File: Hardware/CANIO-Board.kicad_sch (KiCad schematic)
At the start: 0 parts

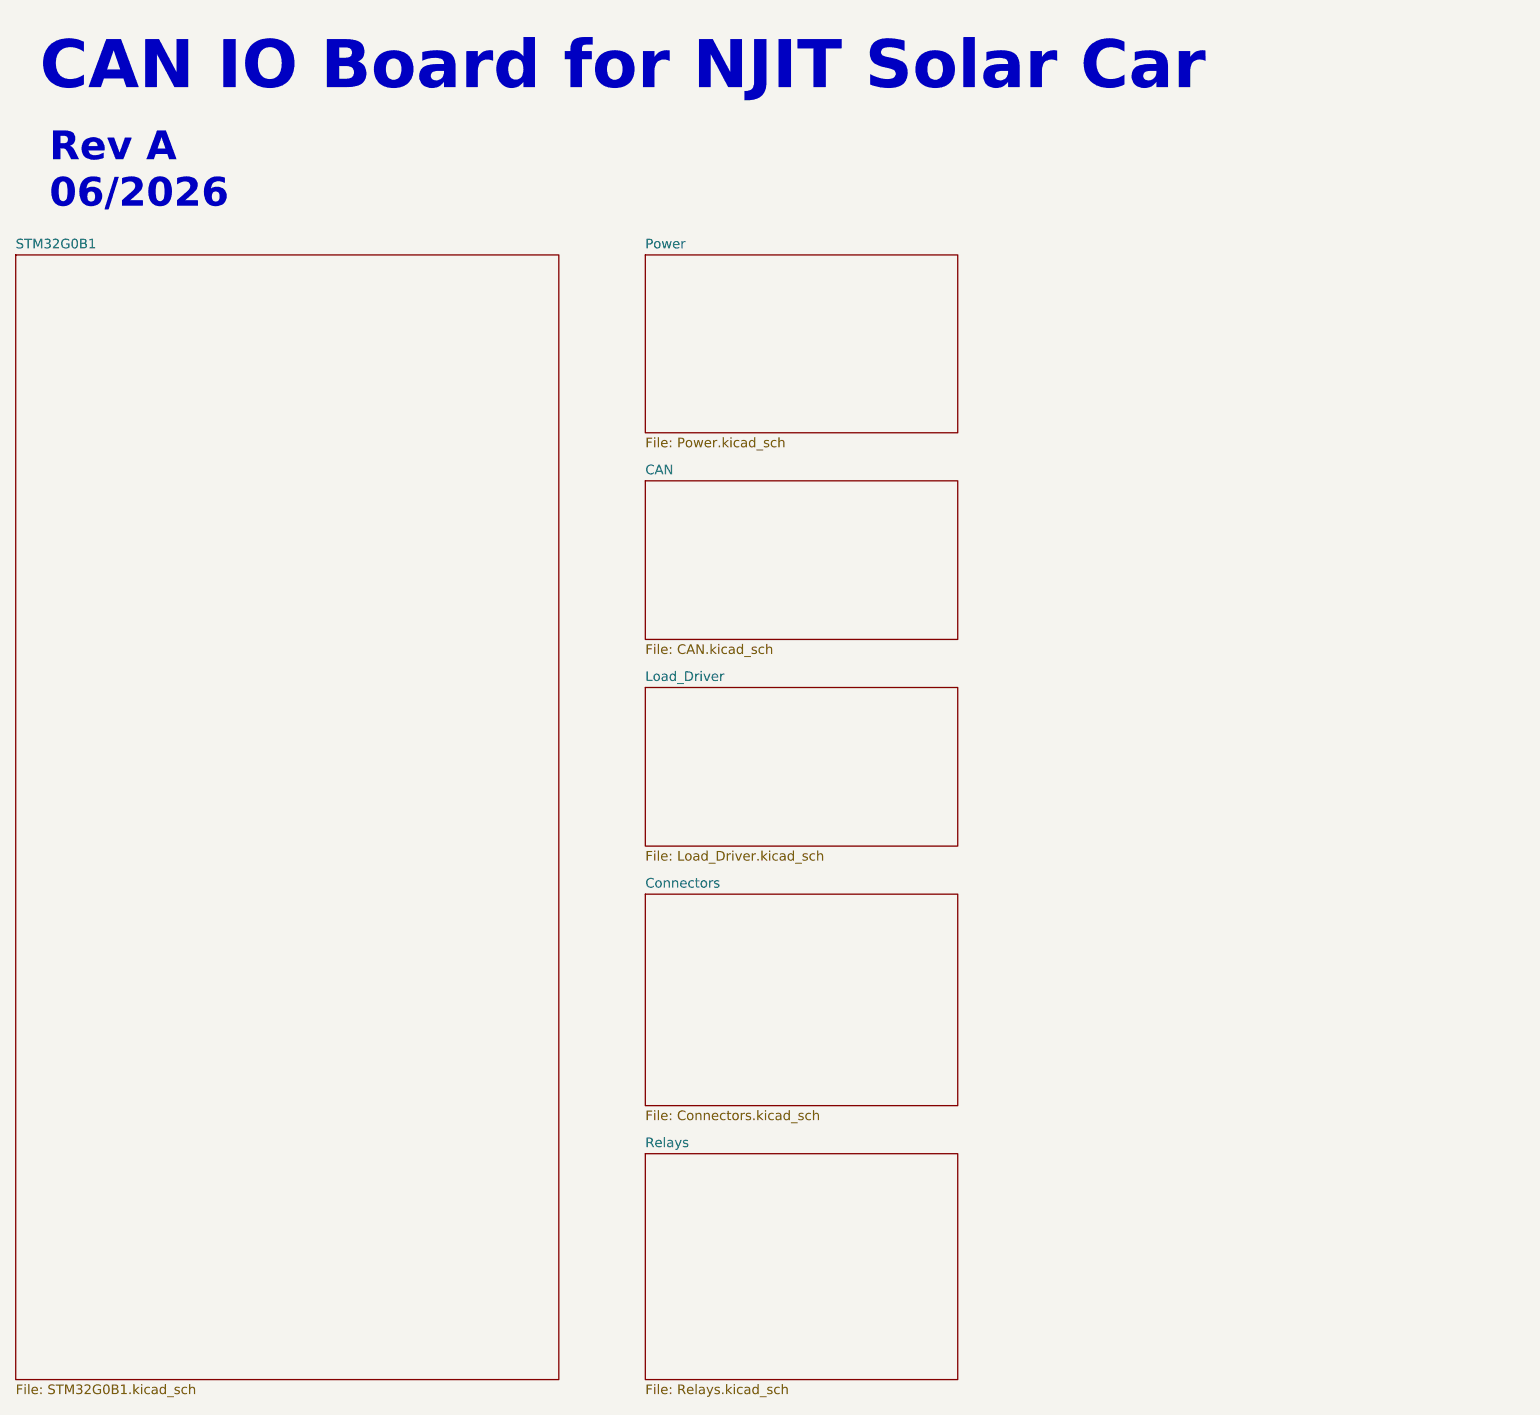
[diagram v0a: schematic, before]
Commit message: Added Relay Driver schematics
- added the ICs, relay sockets, etc
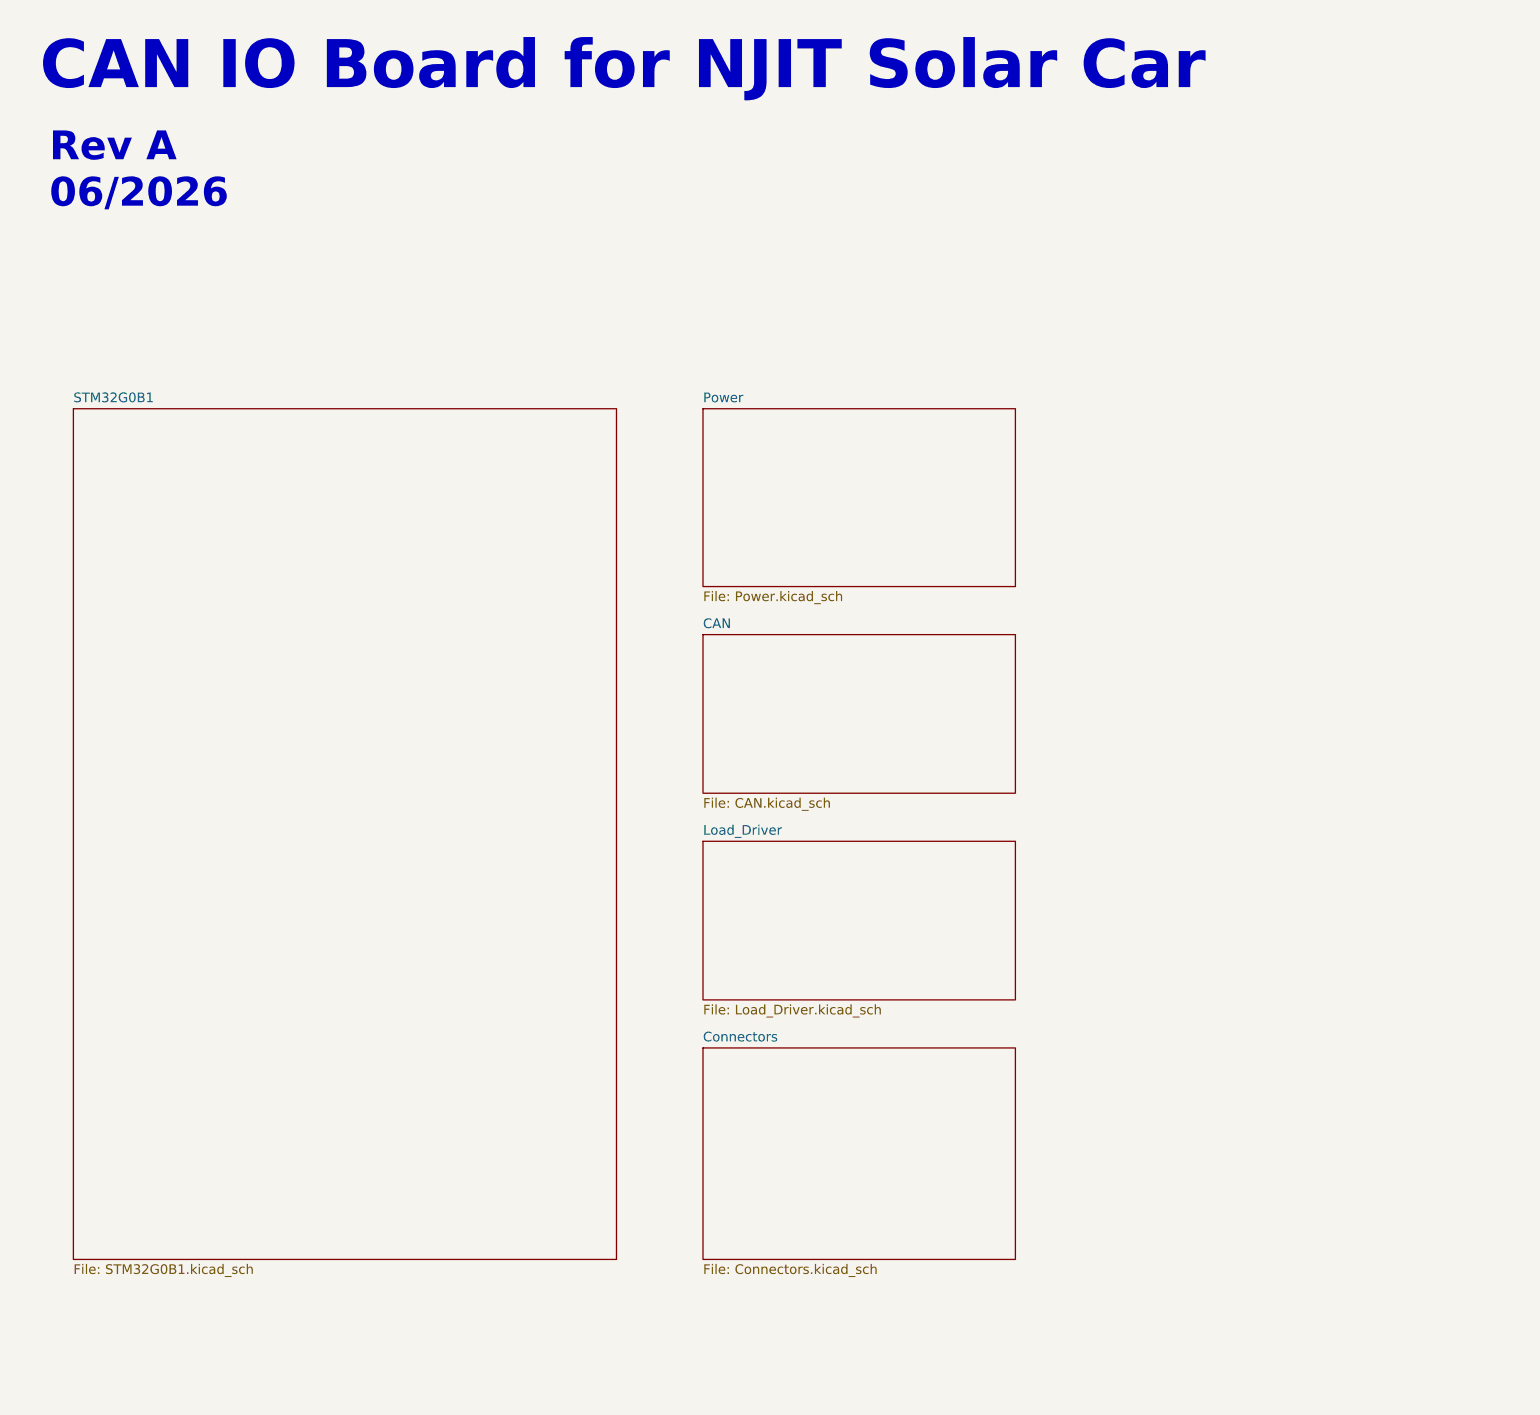
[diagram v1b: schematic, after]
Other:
- removed sheet Relays
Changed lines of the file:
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@@
 	)
 	(sheet
-		(at 100.33 108.585)
+		(at 107.95 128.905)
 		(size 41.275 20.955)
 		(exclude_from_sim no)
@@
 		)
 		(property "Sheetname" "Load_Driver"
-			(at 100.33 107.8734 0)
+			(at 107.95 128.1934 0)
 			(effects
 				(font
@@
 		)
 		(property "Sheetfile" "Load_Driver.kicad_sch"
-			(at 100.33 130.1246 0)
+			(at 107.95 150.4446 0)
 			(effects
 				(font
@@
 	)
 	(sheet
-		(at 17.145 51.435)
-		(size 71.755 148.59)
+		(at 24.765 71.755)
+		(size 71.755 112.395)
 		(exclude_from_sim no)
 		(in_bom yes)
@@
 		)
 		(property "Sheetname" "STM32G0B1"
-			(at 17.145 50.7234 0)
+			(at 24.765 71.0434 0)
 			(effects
 				(font
@@
 		)
 		(property "Sheetfile" "STM32G0B1.kicad_sch"
-			(at 17.145 200.6096 0)
+			(at 24.765 184.7346 0)
 			(effects
 				(font
@@
 	)
 	(sheet
-		(at 100.33 51.435)
+		(at 107.95 71.755)
 		(size 41.275 23.495)
 		(exclude_from_sim no)
@@
 		)
 		(property "Sheetname" "Power"
-			(at 100.33 50.7234 0)
+			(at 107.95 71.0434 0)
 			(effects
 				(font
@@
 		)
 		(property "Sheetfile" "Power.kicad_sch"
-			(at 100.33 75.5146 0)
+			(at 107.95 95.8346 0)
 			(effects
 				(font
@@
 	)
 	(sheet
-		(at 100.33 170.18)
-		(size 41.275 29.845)
-		(exclude_from_sim no)
-		(in_bom yes)
-		(on_board yes)
-		(dnp no)
-		(fields_autoplaced yes)
-		(stroke
-			(width 0.1524)
-			(type solid)
-		)
-		(fill
-			(color 202 202 255 1.0000)
-		)
-		(property "Sheetname" "Relays"
-			(at 100.33 169.4684 0)
-			(effects
-				(font
-					(size 1.27 1.27)
-				)
-				(justify left bottom)
-			)
-		)
-		(property "Sheetfile" "Relays.kicad_sch"
-			(at 100.33 200.6096 0)
-			(effects
-				(font
-					(size 1.27 1.27)
-				)
-				(justify left top)
-			)
-		)
-		(instances
-			(project "CANIO-Board"
-				(path "/a11f98b2-3b09-4cf9-8535-19e509fe91b9"
-					(page "7")
-				)
-			)
-		)
-	)
-	(sheet
-		(at 100.33 135.89)
+		(at 107.95 156.21)
 		(size 41.275 27.94)
 		(exclude_from_sim no)
@@
 		)
 		(property "Sheetname" "Connectors"
-			(at 100.33 135.1784 0)
+			(at 107.95 155.4984 0)
 			(effects
 				(font
@@
 		)
 		(property "Sheetfile" "Connectors.kicad_sch"
-			(at 100.33 164.4146 0)
+			(at 107.95 184.7346 0)
 			(effects
 				(font
@@
 	)
 	(sheet
-		(at 100.33 81.28)
+		(at 107.95 101.6)
 		(size 41.275 20.955)
 		(exclude_from_sim no)
@@
 		)
 		(property "Sheetname" "CAN"
-			(at 100.33 80.5684 0)
+			(at 107.95 100.8884 0)
 			(effects
 				(font
@@
 		)
 		(property "Sheetfile" "CAN.kicad_sch"
-			(at 100.33 102.8196 0)
+			(at 107.95 123.1396 0)
 			(effects
 				(font

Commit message: Finished the ISOW1044 Schematic
- Ported over Kostadin's schematic

Co-authored-by: Kostadin Madjovski <155325994+bivein@users.noreply.github.com>
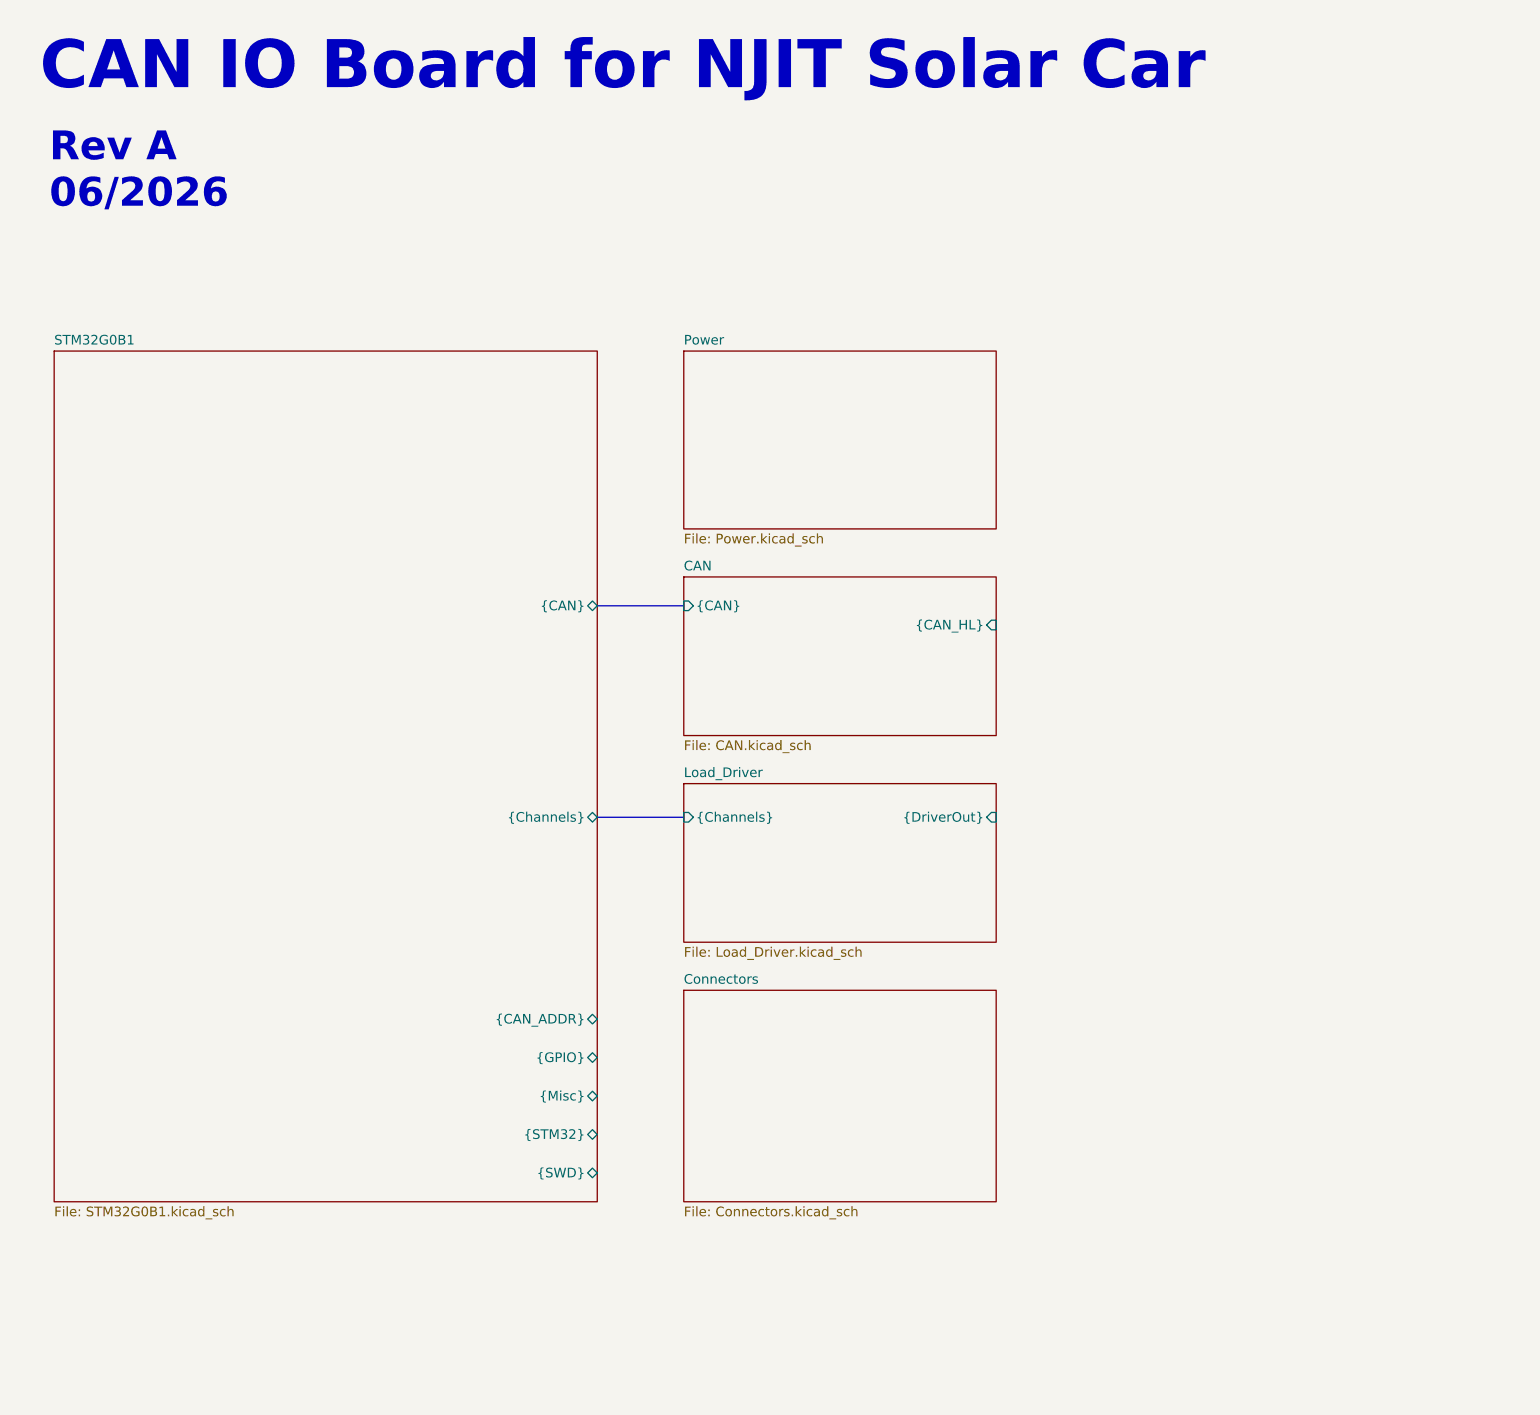
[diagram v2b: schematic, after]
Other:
- sheet CAN ports: added {CAN_HL}, {CAN}; removed none
- sheet Load_Driver ports: added {Channels}, {DriverOut}; removed none
- sheet STM32G0B1 ports: added {CAN_ADDR}, {CAN}, {Channels}, {GPIO}, {Misc}, {STM32}, {SWD}; removed none
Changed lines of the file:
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@@
+		)
+	)
+	(bus
+		(pts
+			(xy 93.98 97.79) (xy 105.41 97.79)
+		)
+		(stroke
+			(width 0)
+			(type default)
+		)
+	)
+	(bus
+		(pts
+			(xy 93.98 125.73) (xy 105.41 125.73)
+		)
+		(stroke
+			(width 0)
+			(type default)
 		)
 	)
@@
 	)
 	(sheet
-		(at 107.95 128.905)
+		(at 105.41 121.285)
 		(size 41.275 20.955)
 		(exclude_from_sim no)
@@
 		)
 		(property "Sheetname" "Load_Driver"
-			(at 107.95 128.1934 0)
+			(at 105.41 120.5734 0)
 			(effects
 				(font
@@
 		)
 		(property "Sheetfile" "Load_Driver.kicad_sch"
-			(at 107.95 150.4446 0)
+			(at 105.41 142.8246 0)
 			(effects
 				(font
@@
 				)
 				(justify left top)
+			)
+		)
+		(pin "{Channels}" input
+			(at 105.41 125.73 180)
+			(effects
+				(font
+					(size 1.27 1.27)
+				)
+				(justify left)
+			)
+		)
+		(pin "{DriverOut}" input
+			(at 146.685 125.73 0)
+			(effects
+				(font
+					(size 1.27 1.27)
+				)
+				(justify right)
 			)
 		)
@@
 	)
 	(sheet
-		(at 24.765 71.755)
+		(at 22.225 64.135)
 		(size 71.755 112.395)
 		(exclude_from_sim no)
@@
 		)
 		(property "Sheetname" "STM32G0B1"
-			(at 24.765 71.0434 0)
+			(at 22.225 63.4234 0)
 			(effects
 				(font
@@
 		)
 		(property "Sheetfile" "STM32G0B1.kicad_sch"
-			(at 24.765 184.7346 0)
+			(at 22.225 177.1146 0)
 			(effects
 				(font
@@
 				)
 				(justify left top)
+			)
+		)
+		(pin "{CAN_ADDR}" bidirectional
+			(at 93.98 152.4 0)
+			(effects
+				(font
+					(size 1.27 1.27)
+				)
+				(justify right)
+			)
+		)
+		(pin "{CAN}" bidirectional
+			(at 93.98 97.79 0)
+			(effects
+				(font
+					(size 1.27 1.27)
+				)
+				(justify right)
+			)
+		)
+		(pin "{Channels}" bidirectional
+			(at 93.98 125.73 0)
+			(effects
+				(font
+					(size 1.27 1.27)
+				)
+				(justify right)
+			)
+		)
+		(pin "{GPIO}" bidirectional
+			(at 93.98 157.48 0)
+			(effects
+				(font
+					(size 1.27 1.27)
+				)
+				(justify right)
+			)
+		)
+		(pin "{Misc}" bidirectional
+			(at 93.98 162.56 0)
+			(effects
+				(font
+					(size 1.27 1.27)
+				)
+				(justify right)
+			)
+		)
+		(pin "{STM32}" bidirectional
+			(at 93.98 167.64 0)
+			(effects
+				(font
+					(size 1.27 1.27)
+				)
+				(justify right)
+			)
+		)
+		(pin "{SWD}" bidirectional
+			(at 93.98 172.72 0)
+			(effects
+				(font
+					(size 1.27 1.27)
+				)
+				(justify right)
 			)
 		)
@@
 	)
 	(sheet
-		(at 107.95 71.755)
+		(at 105.41 64.135)
 		(size 41.275 23.495)
 		(exclude_from_sim no)
@@
 		)
 		(property "Sheetname" "Power"
-			(at 107.95 71.0434 0)
+			(at 105.41 63.4234 0)
 			(effects
 				(font
@@
 		)
 		(property "Sheetfile" "Power.kicad_sch"
-			(at 107.95 95.8346 0)
+			(at 105.41 88.2146 0)
 			(effects
 				(font
@@
 	)
 	(sheet
-		(at 107.95 156.21)
+		(at 105.41 148.59)
 		(size 41.275 27.94)
 		(exclude_from_sim no)
@@
 		)
 		(property "Sheetname" "Connectors"
-			(at 107.95 155.4984 0)
+			(at 105.41 147.8784 0)
 			(effects
 				(font
@@
 		)
 		(property "Sheetfile" "Connectors.kicad_sch"
-			(at 107.95 184.7346 0)
+			(at 105.41 177.1146 0)
 			(effects
 				(font
@@
 	)
 	(sheet
-		(at 107.95 101.6)
+		(at 105.41 93.98)
 		(size 41.275 20.955)
 		(exclude_from_sim no)
@@
 		)
 		(property "Sheetname" "CAN"
-			(at 107.95 100.8884 0)
+			(at 105.41 93.2684 0)
 			(effects
 				(font
@@
 		)
 		(property "Sheetfile" "CAN.kicad_sch"
-			(at 107.95 123.1396 0)
+			(at 105.41 115.5196 0)
 			(effects
 				(font
@@
 			)
 		)
+		(pin "{CAN_HL}" input
+			(at 146.685 100.33 0)
+			(effects
+				(font
+					(size 1.27 1.27)
+				)
+				(justify right)
+			)
+		)
+		(pin "{CAN}" input
+			(at 105.41 97.79 180)
+			(effects
+				(font
+					(size 1.27 1.27)
+				)
+				(justify left)
+			)
+		)
